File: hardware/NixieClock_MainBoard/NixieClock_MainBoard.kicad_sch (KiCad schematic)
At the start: 16 parts, among them J1 Conn_01x14, J2 Conn_01x08, J3 Conn_01x08, J4 Conn_01x08, J5 Conn_01x08

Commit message: change sd card footprint changes on mainboard layout add stl files for display case
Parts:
- added H1, H2, H3, H4, H5, H6: MountingHole, MountingHole:MountingHole_3.2mm_M3, symbol Mechanical:MountingHole
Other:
- note added: "Micro + OP (Für Effekte) - evtl. Radar-Taster.? Sleepmodus. --> Display ausschalten?"
- note removed: "Micro + OP (Für Effekte) BME 280 oder 680 breakout WS28... ein IO vorsehen. ein paar tasten durch Port-Expander - evtl. Radar-Taster.? Sleepmodus. --> Display ausschalten?"

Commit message: V2.0 release fertig.
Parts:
- added H7: MountingHole, MountingHole:MountingHole_3.2mm_M3, symbol Mechanical:MountingHole
- R13, R14, R15, R16, R17, R18, R19, R20, R7, R8: value 10k -> 10R
- R21: value 10k -> 0R0
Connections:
- net A0 is gone; now on net DC: R20.1
- net MOSI: no longer J1.8 (Pin_8), J2.5 (Pin_5), J3.5 (Pin_5), J4.5 (Pin_5), J5.5 (Pin_5)
- new net MOSI_0: J2.5 (Pin_5)
- new net MOSI_1: J3.5 (Pin_5)
- new net MOSI_2: J4.5 (Pin_5)
- new net MOSI_3: J5.5 (Pin_5)
- new net MOSI_4: J1.8 (Pin_8)
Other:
- added sheet SPI_DISPLAY_MOSI (untitled.kicad_sch)
- note removed: "Micro + OP (Für Effekte) - evtl. Radar-Taster.? Sleepmodus. --> Display ausschalten?"

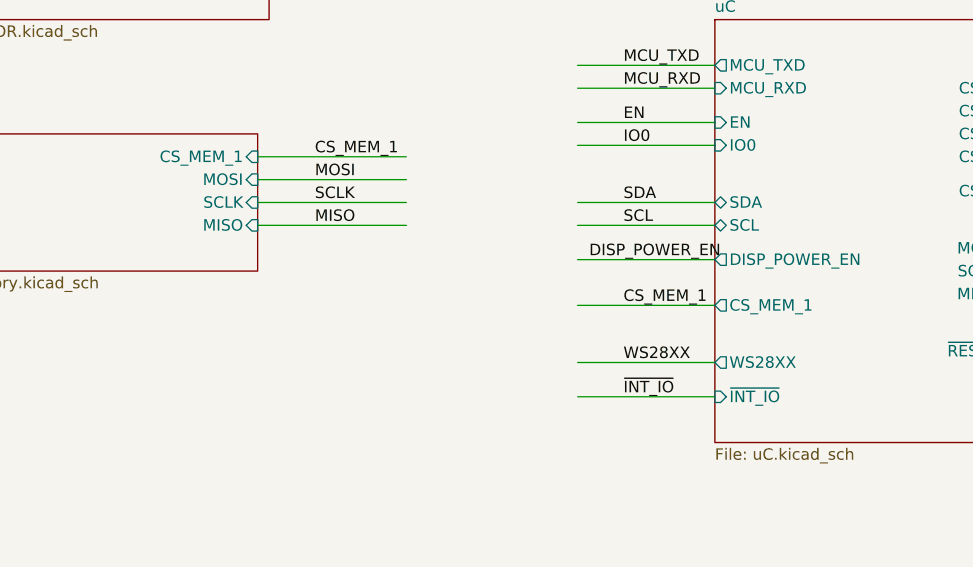
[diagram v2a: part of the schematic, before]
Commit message: Hardware V2.1 add NixieClock_MainBoard/NixieClock_Schematic.pdf
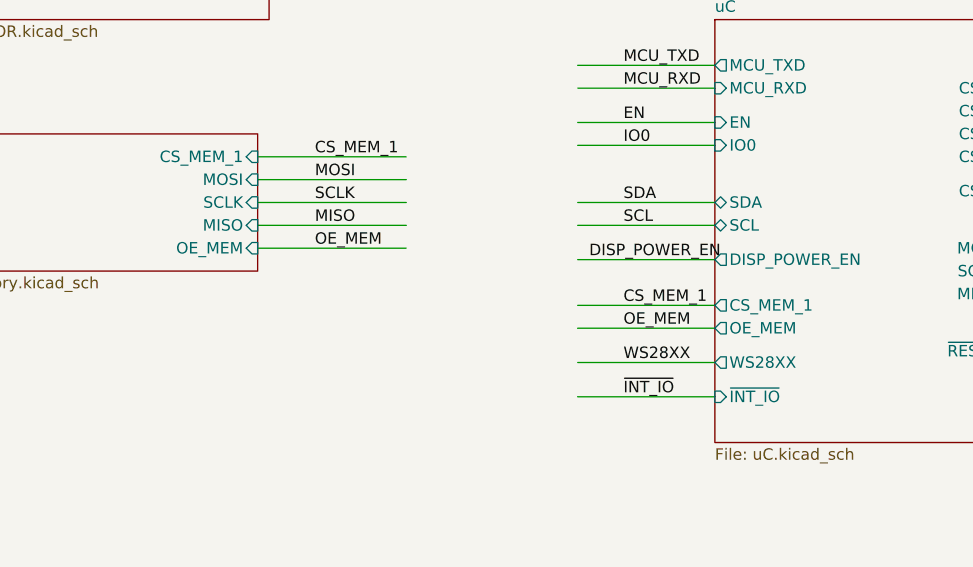
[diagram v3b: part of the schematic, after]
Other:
- sheet memory ports: added OE_MEM; removed none
- sheet uC ports: added OE_MEM; removed none
